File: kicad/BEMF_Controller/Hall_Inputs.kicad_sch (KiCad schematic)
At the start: 9 parts, among them J2 HEADER6, J4 HEADER6

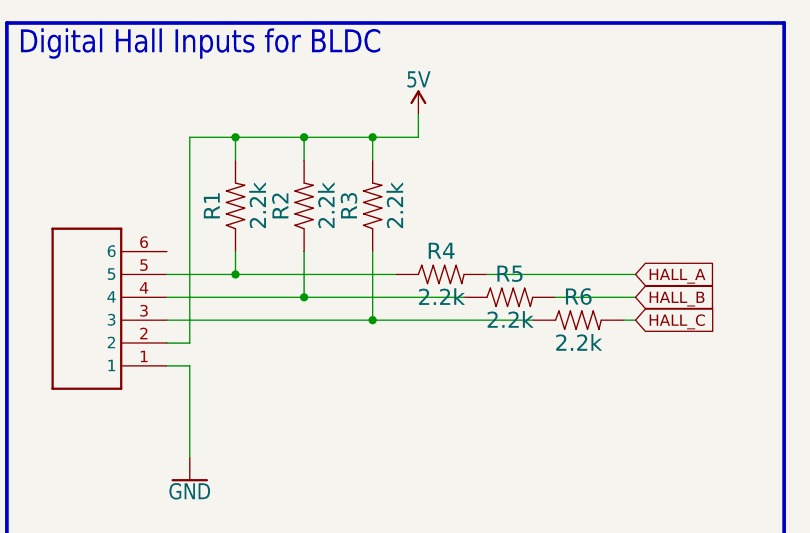
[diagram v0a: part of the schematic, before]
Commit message: Fixed all warnings.
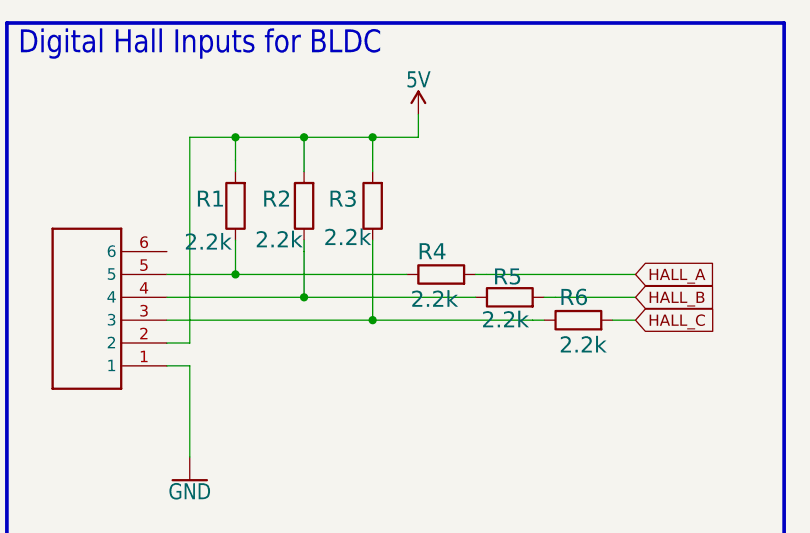
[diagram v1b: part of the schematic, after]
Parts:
- R1, R2, R3, R4, R5, R6: footprint main:1206 -> Resistor_SMD:R_1206_3216Metric; symbol main-eagle-import:RESISTOR1206 -> Component_Library:R2k2

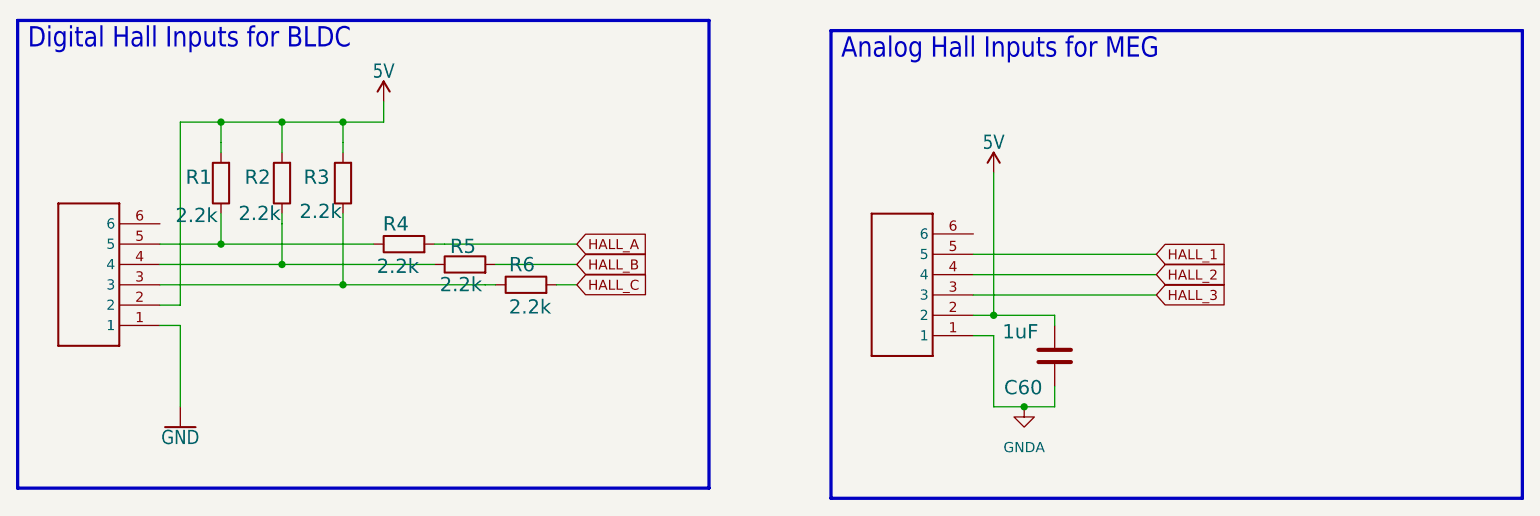
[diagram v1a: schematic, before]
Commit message: Change of plans. Make simple controller for MEG only
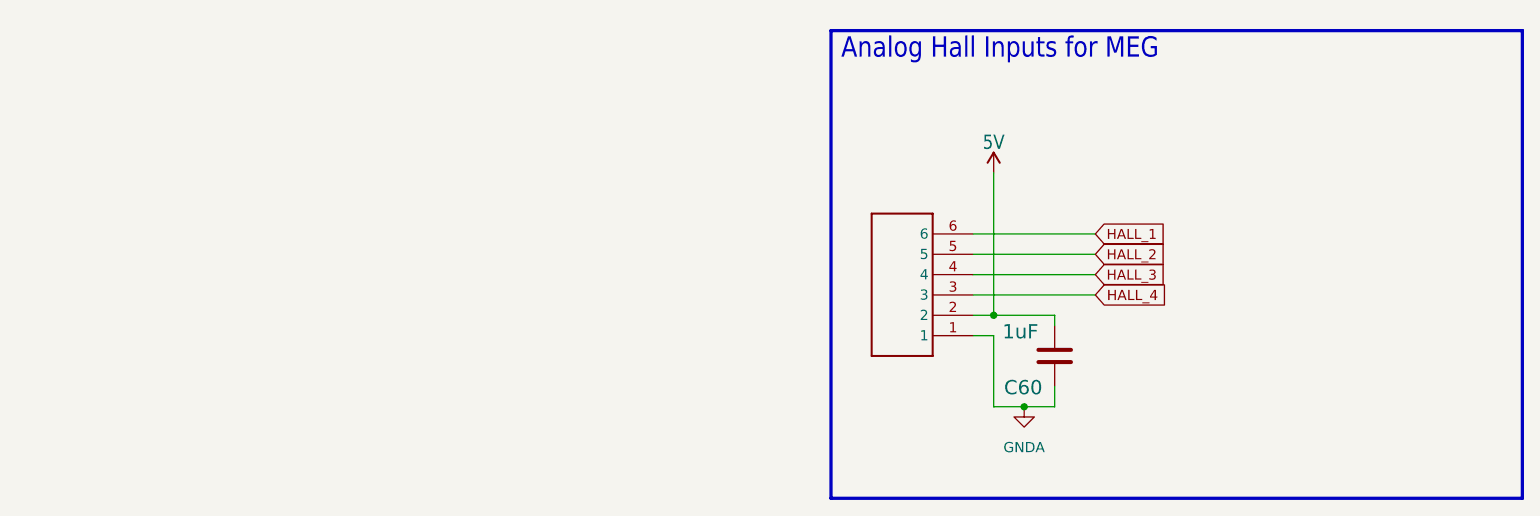
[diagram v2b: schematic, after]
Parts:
- removed J2: HEADER6, main:6PINVALULOK, symbol main-eagle-import:HEADER6
- removed R1, R2, R3, R4, R5, R6: 2.2k, Resistor_SMD:R_1206_3216Metric, symbol Component_Library:R2k2
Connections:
- net HALL_1: now also J4.6; no longer J4.5
- net HALL_2: now also J4.5; no longer J4.4
- net HALL_3: now also J4.4; no longer J4.3
- new net HALL_4: J4.3
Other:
- note removed: "Digital Hall Inputs for BLDC"
